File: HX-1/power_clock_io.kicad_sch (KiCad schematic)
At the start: 0 parts

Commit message: move components to correct sheets, change net labels to global
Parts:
- added C22, C23: 10pF, Capacitor_SMD:C_0603_1608Metric, symbol Device:C
- added J1: Conn_01x02_Socket, symbol Connector:Conn_01x02_Socket
- added Y1: 16MHz, Crystal:Crystal_SMD_3225-4Pin_3.2x2.5mm, symbol Device:Crystal_GND24
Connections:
- new net +5V: J1.1 (Pin_1)
- new net GND: C22.1, C23.2, J1.2 (Pin_2), Y1.2, Y1.4
- new net RCC_OSC_IN: C22.2, Y1.1
- new net RCC_OSC_OUT: C23.1, Y1.3
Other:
- note added: "(Load_C (10pF) - Stray_C (~5pF) ) * 2 = 10 pF"

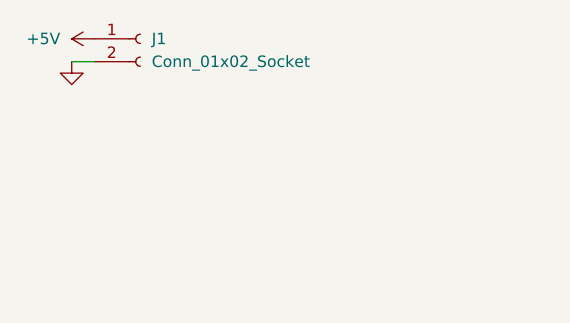
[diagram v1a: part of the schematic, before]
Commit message: add first draft of USB C design
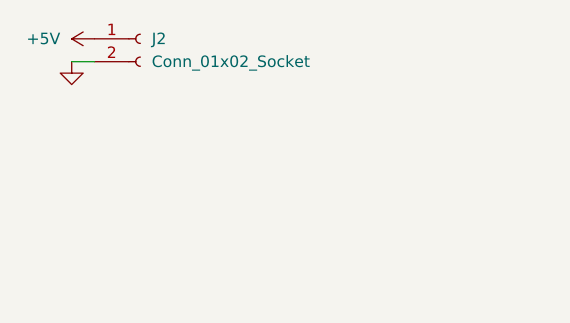
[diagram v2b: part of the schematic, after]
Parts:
- renumbered J1 to J2
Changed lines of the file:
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@@
 		(dnp no)
 		(fields_autoplaced yes)
-		(property "Reference" "J1"
+		(property "Reference" "J2"
 			(at 27.94 20.3199 0)
 			(effects
@@
 			(project "HX-1"
 				(path "/a3219989-2bf1-44ea-9412-fab86edfb39b/3a90d823-0fb3-4447-b918-f2095473f7ca"
-					(reference "J1")
+					(reference "J2")
 					(unit 1)
 				)

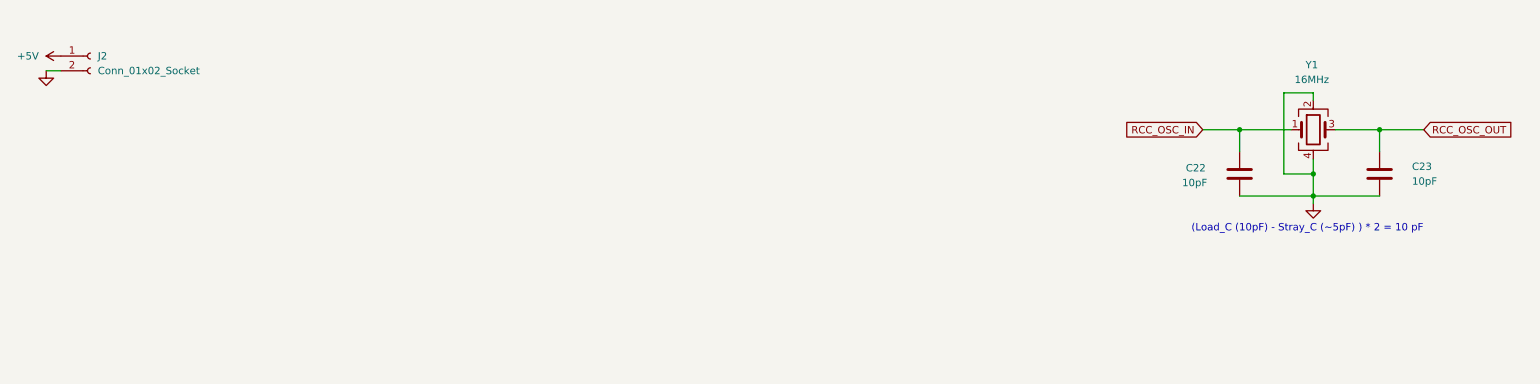
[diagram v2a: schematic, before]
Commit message: add vbus filtering and voltage regululator for 3.3V
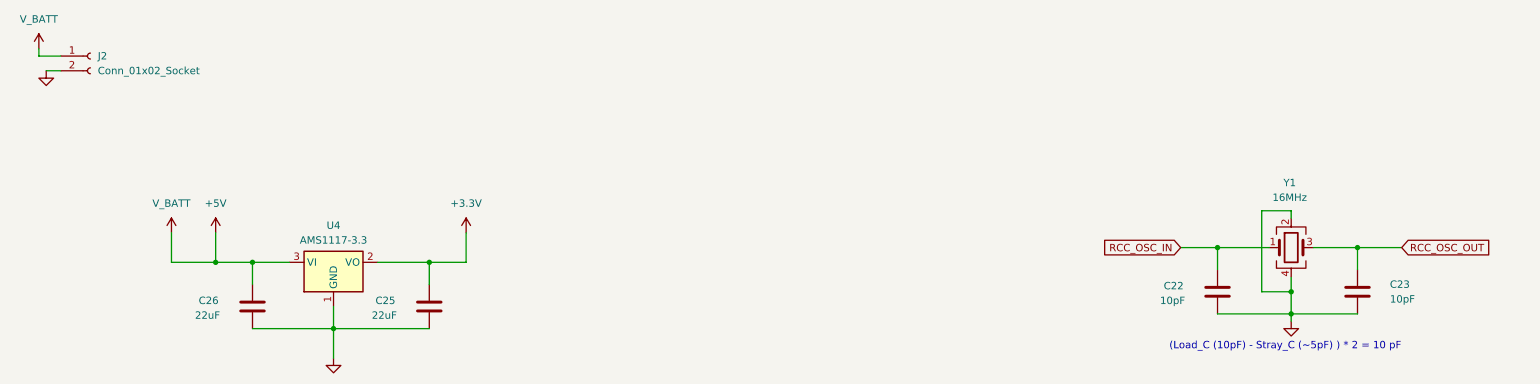
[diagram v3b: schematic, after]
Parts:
- added C25, C26: 22uF, Capacitor_SMD:C_0603_1608Metric, symbol Device:C
- added U4: AMS1117-3.3, Package_TO_SOT_SMD:SOT-223-3_TabPin2, symbol Regulator_Linear:AMS1117-3.3
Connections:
- net +5V: now also C26.2, U4.3 (VI)
- net GND: now also C25.1, C26.1, U4.1 (GND)
- new net +3.3V: C25.2, U4.2 (VO)
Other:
- moved on the sheet: C22, C23, Y1

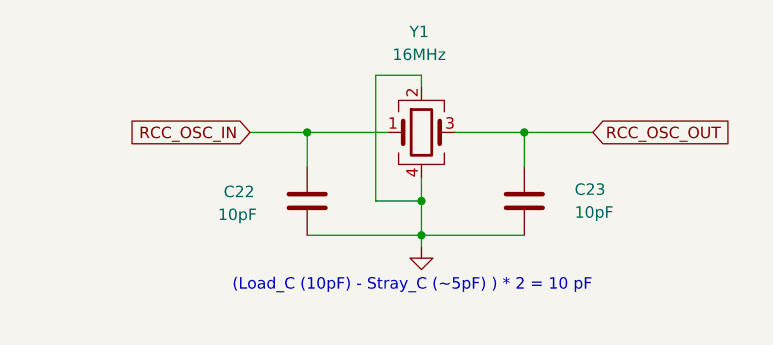
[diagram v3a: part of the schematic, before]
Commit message: change almost all components to be basic jlcpcb parts
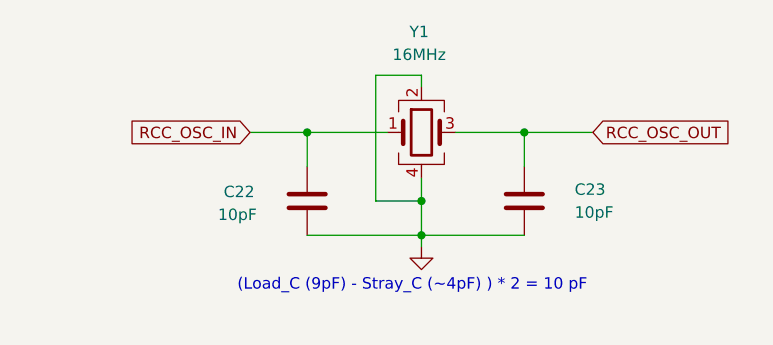
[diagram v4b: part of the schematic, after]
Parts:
- C22, C23: LCSC PN C338151 -> C1634
- C25, C26: LCSC PN C338151 -> C59461
- Y1: LCSC PN C112972 -> C13738
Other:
- note added: "(Load_C (9pF) - Stray_C (~4pF) ) * 2 = 10 pF"
- note removed: "(Load_C (10pF) - Stray_C (~5pF) ) * 2 = 10 pF"
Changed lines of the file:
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@@
 		)
 	)
-	(text "(Load_C (10pF) - Stray_C (~5pF) ) * 2 = 10 pF"
+	(text "(Load_C (9pF) - Stray_C (~4pF) ) * 2 = 10 pF"
 		(exclude_from_sim no)
 		(at 232.664 70.358 0)
@@
 			)
 		)
-		(property "LCSC PN" "C338151"
+		(property "LCSC PN" "C1634"
 			(at 220.98 60.96 0)
 			(effects
@@
 			)
 		)
-		(property "LCSC PN" "C338151"
+		(property "LCSC PN" "C59461"
 			(at 54.61 63.5 0)
 			(effects
@@
 			)
 		)
-		(property "LCSC PN" "C338151"
+		(property "LCSC PN" "C59461"
 			(at 85.09 63.5 0)
 			(effects
@@
 			)
 		)
-		(property "LCSC PN" "C112972"
+		(property "LCSC PN" "C13738"
 			(at 233.68 53.34 0)
 			(effects
@@
 			)
 		)
-		(property "LCSC PN" "C338151"
+		(property "LCSC PN" "C1634"
 			(at 245.11 60.96 0)
 			(effects

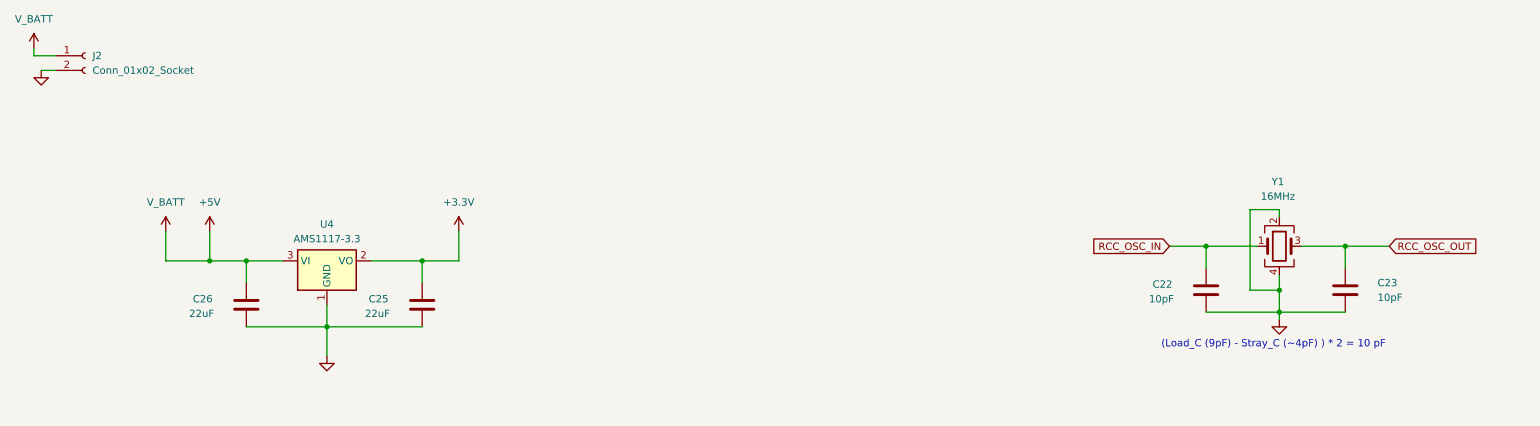
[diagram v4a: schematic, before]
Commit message: add battery input circuit
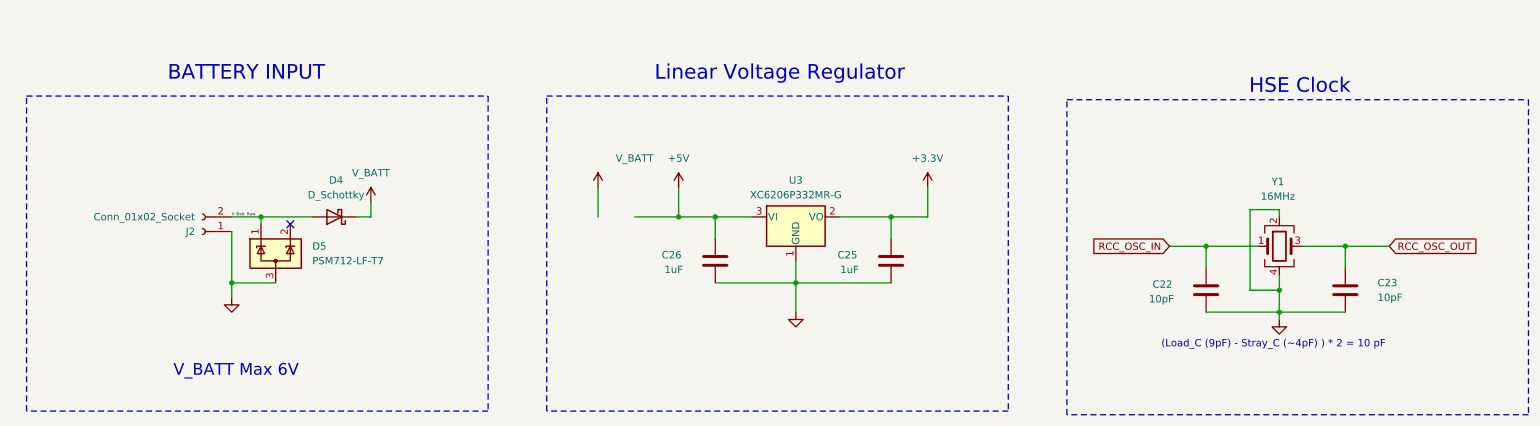
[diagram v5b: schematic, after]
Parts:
- removed U4: AMS1117-3.3, Package_TO_SOT_SMD:SOT-223-3_TabPin2, symbol Regulator_Linear:AMS1117-3.3
- added D4: D_Schottky, Diode_SMD:D_SOD-323F, symbol Device:D_Schottky
- added D5: PSM712-LF-T7, Package_TO_SOT_SMD:SOT-23-3, symbol Power_Protection:ESDA5V3L
- added U3: XC6206P332MR-G, Package_TO_SOT_SMD:SOT-23-3, symbol Regulator_Linear:XC6206PxxxMR
- C25, C26: value 22uF -> 1uF; LCSC PN C59461 -> C15849
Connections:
- net +3.3V: now also U3.2 (VO)
- net +5V: now also U3.3 (VI); no longer J2.1 (Pin_1)
- net GND: now also J2.1 (Pin_1), D5.3 (A), U3.1 (GND); no longer J2.2 (Pin_2)
- new net V_BATT: D4.1 (K)
- new net V_Batt_Raw: D4.2 (A), D5.1 (K), J2.2 (Pin_2)
- no-connect marks 0 -> 1
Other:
- note added: "BATTERY INPUT"
- note added: "HSE Clock"
- note added: "Linear Voltage Regulator"
- note added: "V_BATT Max 6V"
- moved on the sheet: C25, C26, J2

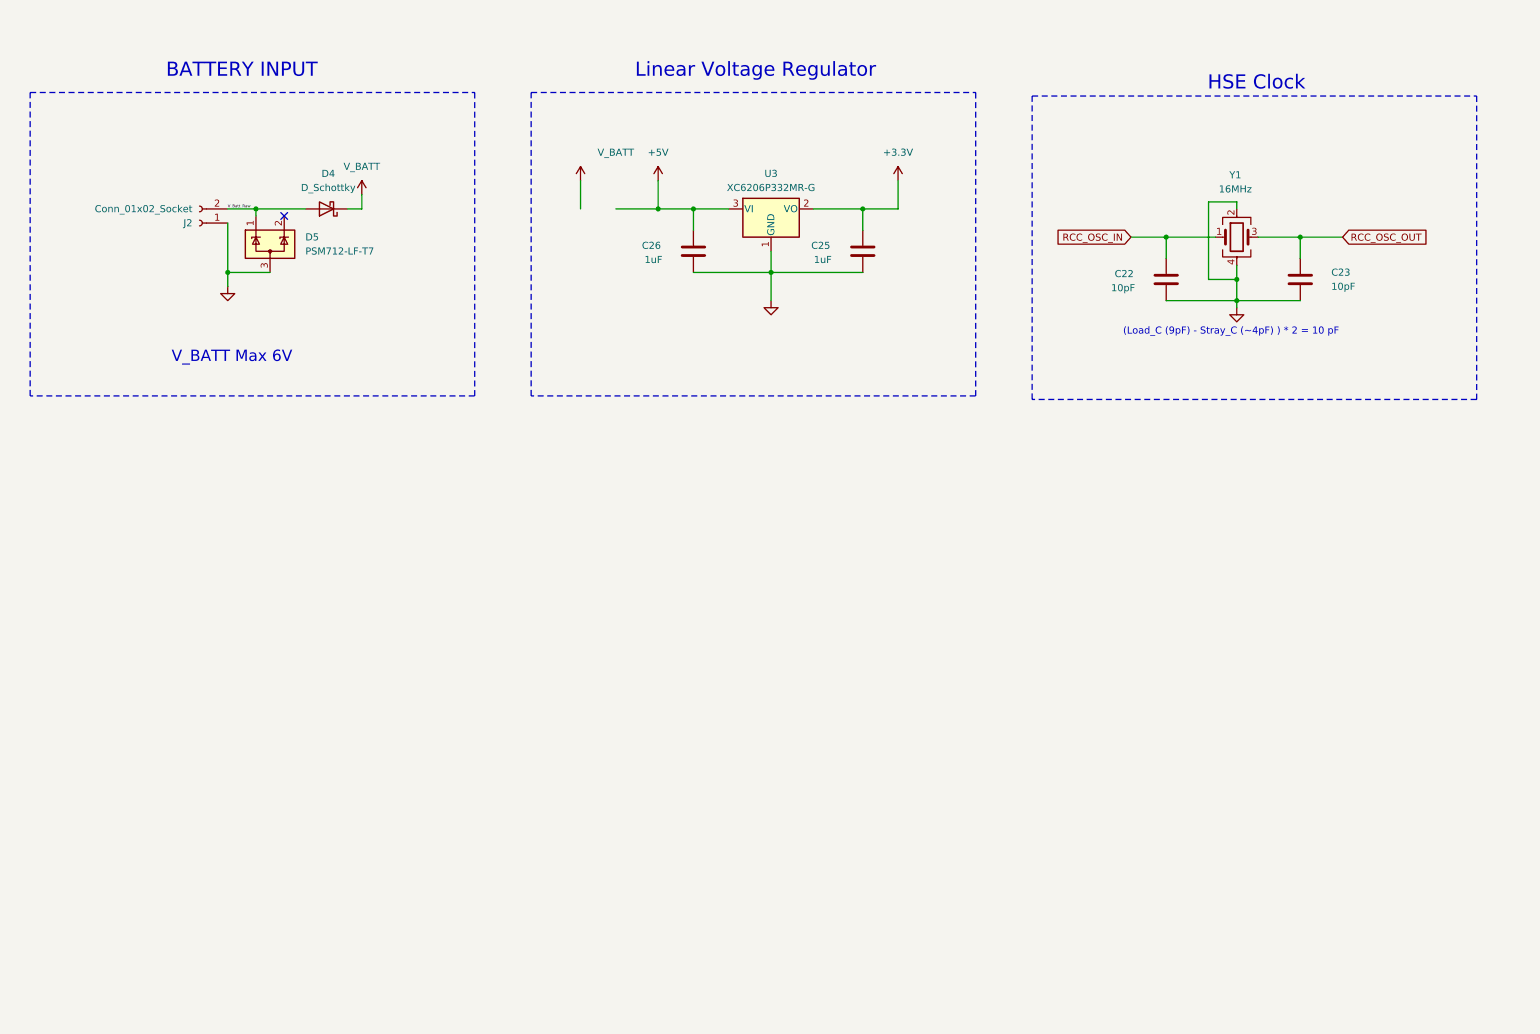
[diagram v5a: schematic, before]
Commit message: add buzzer, remove one ADC diff pair
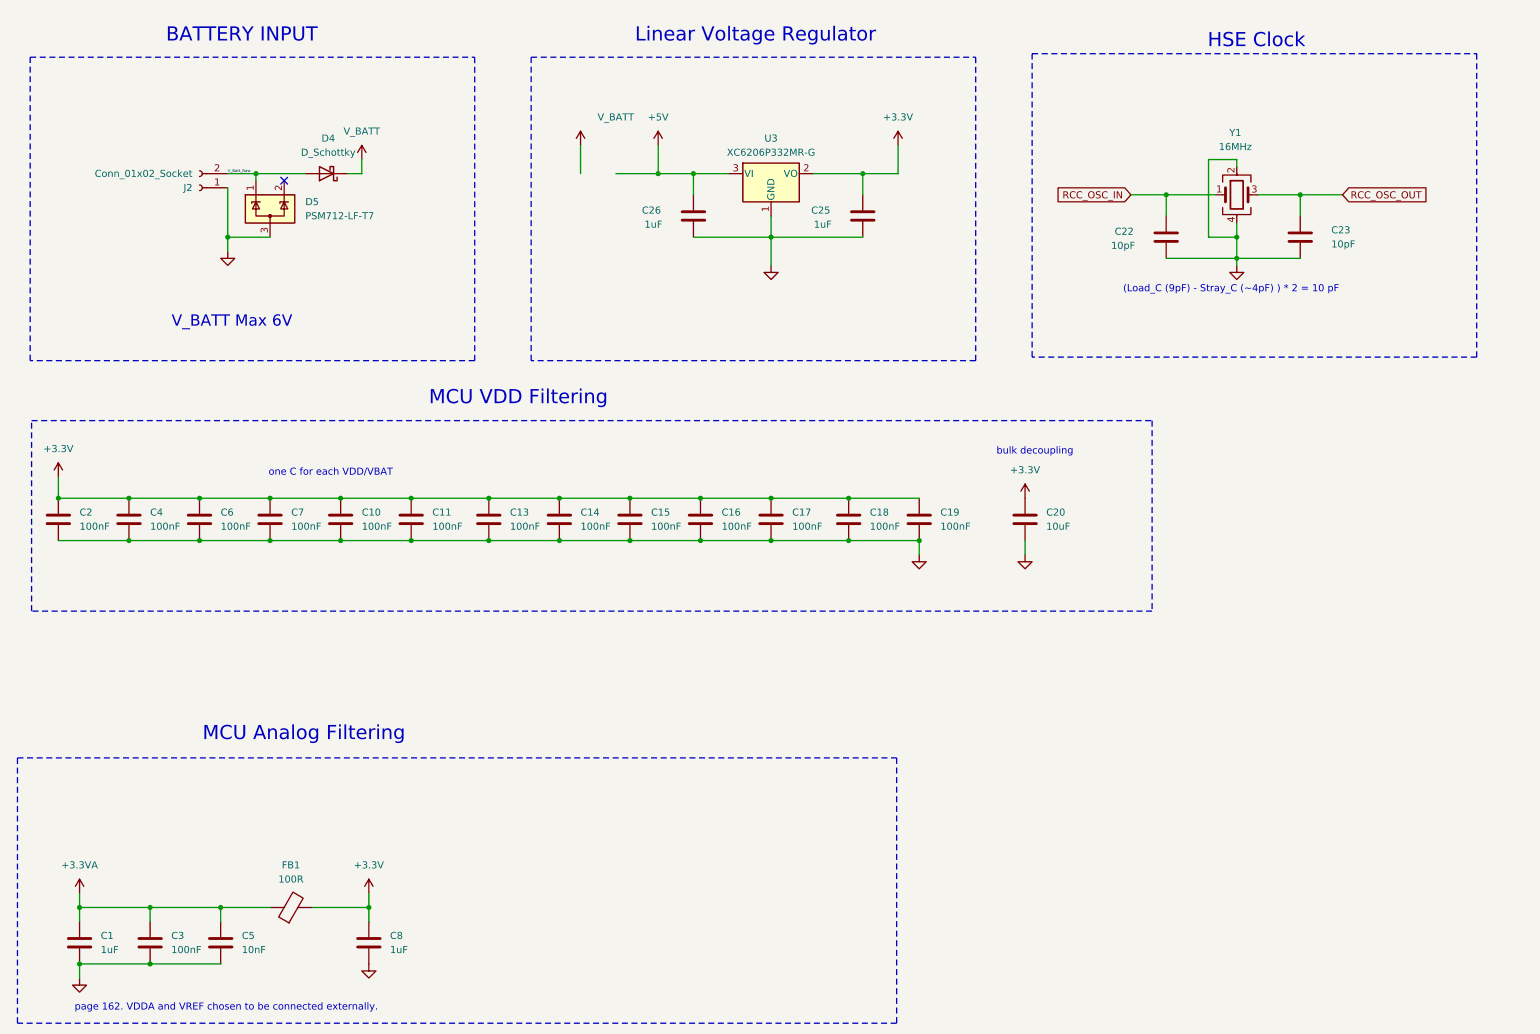
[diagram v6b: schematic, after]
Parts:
- added C1, C8: 1uF, Capacitor_SMD:C_0603_1608Metric, symbol Device:C
- added C10, C11, C13, C14, C15, C16, C17, C18, C19, C2, C3, C4, C6, C7: 100nF, Capacitor_SMD:C_0603_1608Metric, symbol Device:C
- added C20: 10uF, Capacitor_SMD:C_0603_1608Metric, symbol Device:C
- added C5: 10nF, Capacitor_SMD:C_0603_1608Metric, symbol Device:C
- added FB1: 100R, Resistor_SMD:R_0805_2012Metric, symbol Device:FerriteBead
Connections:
- net +3.3V: now also C10.1, C11.1, C13.1, C14.1, C15.1, C16.1, C17.1, C18.1, C19.1, C2.1, C20.1, C4.1, C6.1, C7.1, C8.1, FB1.2
- net GND: now also C1.2, C10.2, C11.2, C13.2, C14.2, C15.2, C16.2, C17.2, C18.2, C19.2, C2.2, C20.2, C3.2, C4.2, C5.2, C6.2, C7.2, C8.2
- new net +3.3VA: C1.1, C3.1, C5.1, FB1.1
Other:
- note added: "MCU Analog Filtering"
- note added: "MCU VDD Filtering"
- note added: "bulk decoupling"
- note added: "one C for each VDD/VBAT"
- note added: "page 162. VDDA and VREF chosen to be connected externally."
- moved on the sheet: C22, C23, C25, C26, D4, D5, J2, U3, Y1

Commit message: remove uart7, spi2 and extra CS. Not needed. Start mapping GPIO
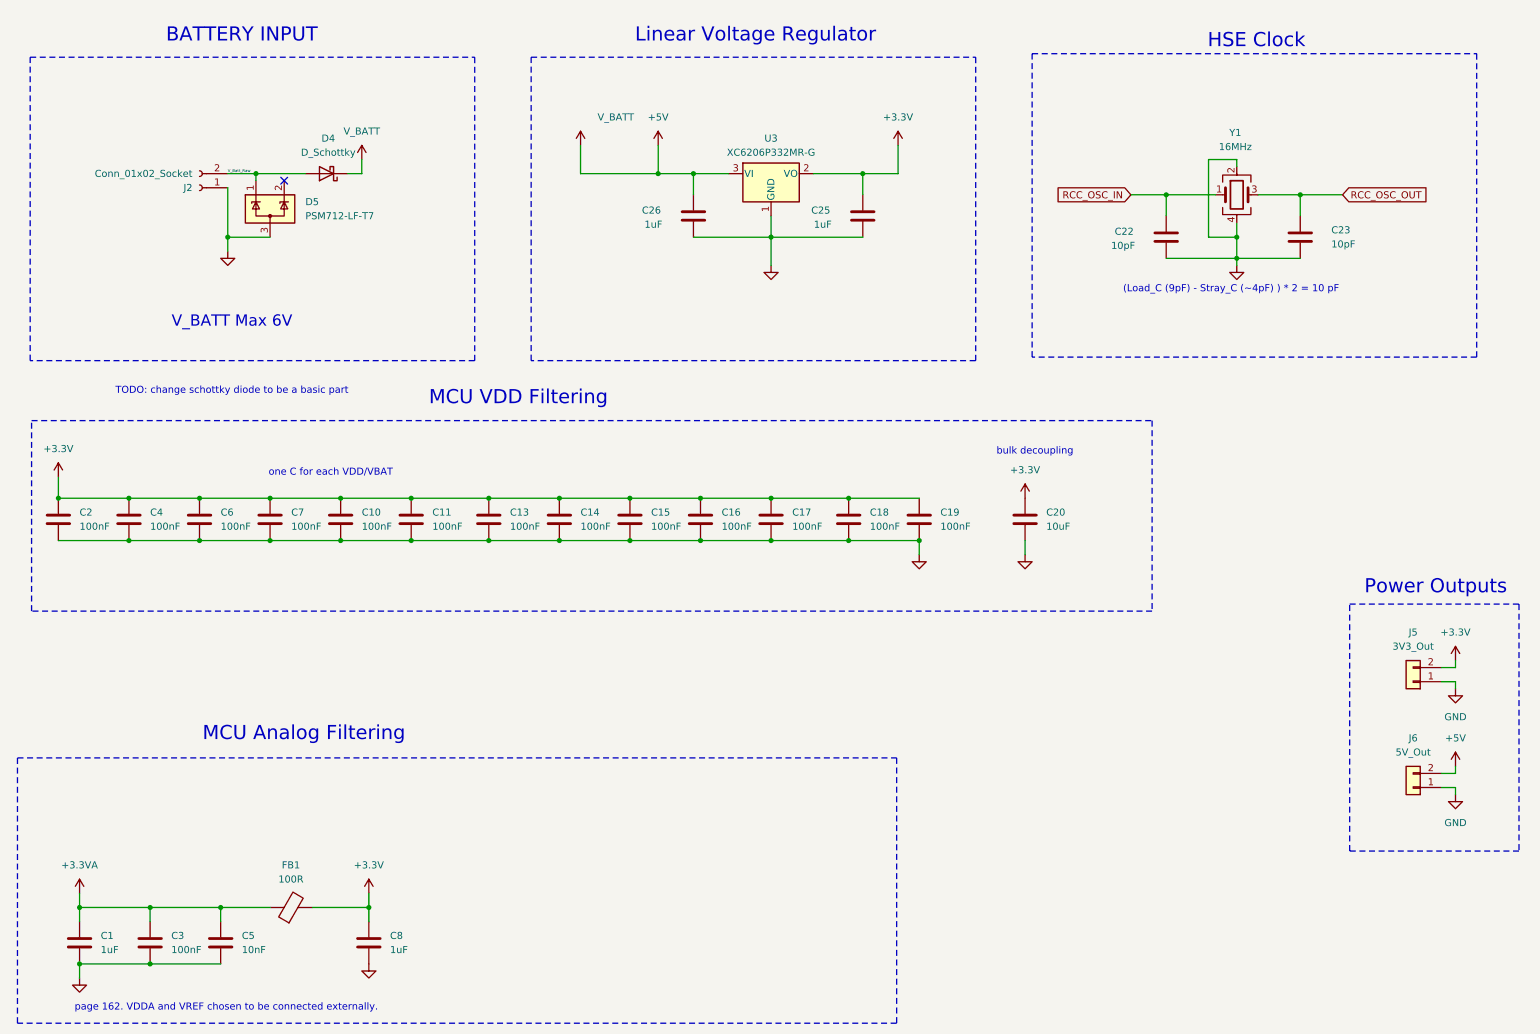
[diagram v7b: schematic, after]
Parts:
- added J5: 3V3_Out, symbol Connector_Generic:Conn_01x02
- added J6: 5V_Out, symbol Connector_Generic:Conn_01x02
- J2: footprint (none) -> Connector_JST:JST_PH_B2B-PH-K_1x02_P2.00mm_Vertical
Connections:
- net V_BATT is gone; now on net +5V: D4.1 (K)
- net +3.3V: now also J5.2 (Pin_2)
- net +5V: now also J6.2 (Pin_2)
- net GND: now also J5.1 (Pin_1), J6.1 (Pin_1)
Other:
- note added: "Power Outputs"
- note added: "TODO: change schottky diode to be a basic part"
